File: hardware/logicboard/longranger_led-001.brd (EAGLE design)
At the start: 12.7 x 25.4 mm, 4 parts, among them J1 LED

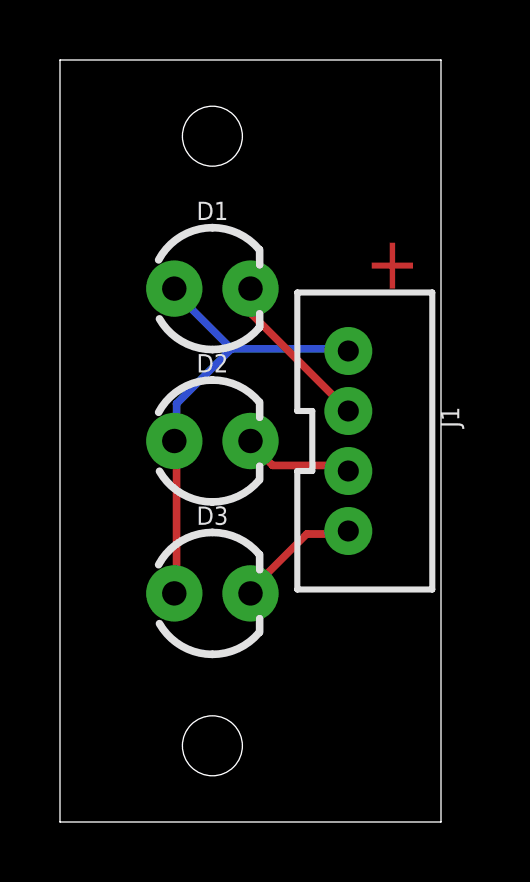
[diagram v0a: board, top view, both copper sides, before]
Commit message: Changed layout.
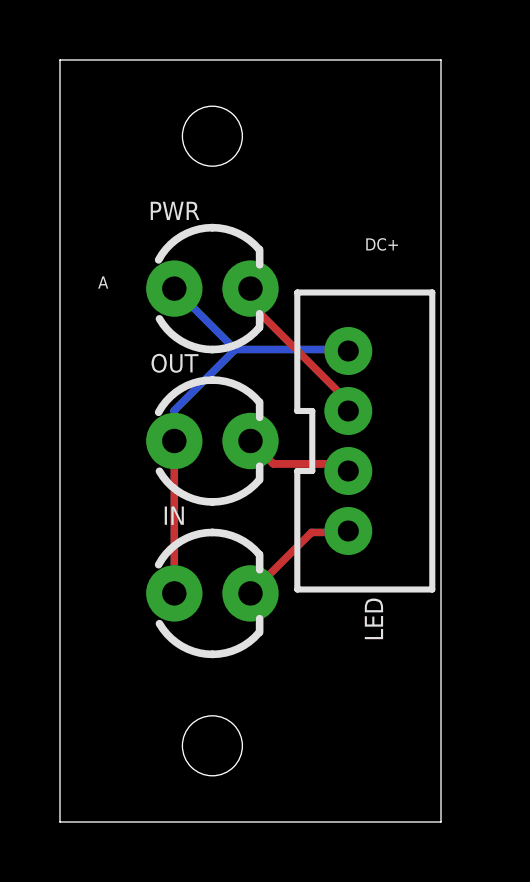
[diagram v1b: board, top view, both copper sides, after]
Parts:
- IN: value IN -> (none)
- LED: value LED -> (none)
- OUT: value OUT -> (none)
- PWR: value PWR -> (none)
- renumbered D1 to PWR, D2 to OUT, D3 to IN, J1 to LED
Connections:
- net N$4 renamed PWR
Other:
- board text added: "A"
- board text added: "DC+"
- board text removed: "+"
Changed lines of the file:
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@@
 <setting verticaltext="up"/>
 </settings>
-<grid distance="0.1" unitdist="inch" unit="inch" style="dots" multiple="1" display="yes" altdistance="0.025" altunitdist="inch" altunit="inch"/>
+<grid distance="50" unitdist="mil" unit="mil" style="lines" multiple="2" display="yes" altdistance="0.025" altunitdist="inch" altunit="inch"/>
 <layers>
 <layer number="1" name="Top" color="4" fill="1" visible="yes" active="yes"/>
@@
 <layer number="25" name="tNames" color="7" fill="1" visible="yes" active="yes"/>
 <layer number="26" name="bNames" color="7" fill="1" visible="yes" active="yes"/>
-<layer number="27" name="tValues" color="7" fill="1" visible="yes" active="yes"/>
-<layer number="28" name="bValues" color="7" fill="1" visible="yes" active="yes"/>
+<layer number="27" name="tValues" color="7" fill="1" visible="no" active="yes"/>
+<layer number="28" name="bValues" color="7" fill="1" visible="no" active="yes"/>
 <layer number="29" name="tStop" color="7" fill="3" visible="yes" active="yes"/>
 <layer number="30" name="bStop" color="7" fill="6" visible="yes" active="yes"/>
@@
 <hole x="5.08" y="2.54" drill="1.99898125"/>
 <hole x="5.08" y="22.86" drill="1.99898125"/>
-<text x="10.16" y="17.78" size="1.778" layer="1">+</text>
+<text x="10.16" y="19.05" size="0.4064" layer="25">DC+</text>
+<text x="1.27" y="17.78" size="0.4064" layer="25">A</text>
 </plain>
 <attributes>
@@
 </autorouter>
 <elements>
-<element name="J1" library="SparkFun-Connectors" package="JST-4-PTH-VERT" value="LED" x="10.16" y="12.7" rot="R270">
+<element name="LED" library="SparkFun-Connectors" package="JST-4-PTH-VERT" value="" x="10.16" y="12.7" smashed="yes" rot="R270">
+<attribute name="NAME" x="10.16" y="7.493" size="0.6096" layer="25" font="vector" ratio="20" rot="R270"/>
 <attribute name="PROD_ID" value="CONN-13251" x="10.16" y="12.7" size="1.778" layer="27" rot="R270" display="off"/>
+<attribute name="VALUE" x="6.858" y="14.351" size="0.6096" layer="27" font="vector" ratio="20" rot="R270"/>
 </element>
-<element name="D1" library="SparkFun-LED" package="LED_3MM" value="PWR" x="5.08" y="17.78">
+<element name="PWR" library="SparkFun-LED" package="LED_3MM" value="" x="5.08" y="17.78" smashed="yes">
+<attribute name="NAME" x="3.81" y="20.066" size="0.6096" layer="25" font="vector" ratio="20" align="bottom-center"/>
 <attribute name="PROD_ID" value="DIO-08794" x="5.08" y="17.78" size="1.778" layer="27" display="off"/>
+<attribute name="VALUE" x="5.08" y="15.494" size="0.6096" layer="27" font="vector" ratio="20" align="top-center"/>
 </element>
-<element name="D2" library="SparkFun-LED" package="LED_3MM" value="OUT" x="5.08" y="12.7">
+<element name="OUT" library="SparkFun-LED" package="LED_3MM" value="" x="5.08" y="12.7" smashed="yes">
+<attribute name="NAME" x="3.81" y="14.986" size="0.6096" layer="25" font="vector" ratio="20" align="bottom-center"/>
 <attribute name="PROD_ID" value="DIO-08794" x="5.08" y="12.7" size="1.778" layer="27" display="off"/>
+<attribute name="VALUE" x="5.08" y="10.414" size="0.6096" layer="27" font="vector" ratio="20" align="top-center"/>
 </element>
-<element name="D3" library="SparkFun-LED" package="LED_3MM" value="IN" x="5.08" y="7.62">
+<element name="IN" library="SparkFun-LED" package="LED_3MM" value="" x="5.08" y="7.62" smashed="yes">
+<attribute name="NAME" x="3.81" y="9.906" size="0.6096" layer="25" font="vector" ratio="20" align="bottom-center"/>
 <attribute name="PROD_ID" value="DIO-08794" x="5.08" y="7.62" size="1.778" layer="27" display="off"/>
+<attribute name="VALUE" x="5.08" y="5.334" size="0.6096" layer="27" font="vector" ratio="20" align="top-center"/>
 </element>
 </elements>
 <signals>
-<signal name="N$4">
-<contactref element="J1" pad="1"/>
-<contactref element="D3" pad="A"/>
-<contactref element="D2" pad="A"/>
-<contactref element="D1" pad="A"/>
-<wire x1="3.8862" y1="12.573" x2="3.8862" y2="7.7724" width="0.254" layer="1"/>
-<wire x1="3.8862" y1="7.7724" x2="3.81" y2="7.62" width="0.254" layer="1"/>
-<wire x1="3.8862" y1="12.573" x2="3.81" y2="12.7" width="0.254" layer="1"/>
-<wire x1="5.715" y1="15.7734" x2="9.6012" y2="15.7734" width="0.254" layer="16"/>
-<wire x1="3.8862" y1="17.6022" x2="5.715" y2="15.7734" width="0.254" layer="16"/>
-<wire x1="9.6012" y1="15.7734" x2="9.61" y2="15.7" width="0.254" layer="16"/>
-<wire x1="3.8862" y1="17.6022" x2="3.81" y2="17.78" width="0.254" layer="16"/>
-<wire x1="3.8862" y1="13.9446" x2="3.8862" y2="12.8016" width="0.254" layer="16"/>
-<wire x1="5.715" y1="15.7734" x2="3.8862" y2="13.9446" width="0.254" layer="16"/>
-<wire x1="3.8862" y1="12.8016" x2="3.81" y2="12.7" width="0.254" layer="16"/>
+<signal name="PWR">
+<contactref element="LED" pad="1"/>
+<contactref element="IN" pad="A"/>
+<contactref element="OUT" pad="A"/>
+<contactref element="PWR" pad="A"/>
+<wire x1="3.81" y1="12.7" x2="3.81" y2="7.62" width="0.254" layer="1"/>
+<wire x1="5.842" y1="15.748" x2="9.398" y2="15.748" width="0.254" layer="16"/>
+<wire x1="3.81" y1="17.78" x2="5.842" y2="15.748" width="0.254" layer="16"/>
+<wire x1="9.398" y1="15.748" x2="9.61" y2="15.7" width="0.254" layer="16"/>
+<wire x1="3.81" y1="13.716" x2="3.81" y2="12.7" width="0.254" layer="16"/>
+<wire x1="5.842" y1="15.748" x2="3.81" y2="13.716" width="0.254" layer="16"/>
 </signal>
 <signal name="N$5">
-<contactref element="J1" pad="2"/>
-<contactref element="D1" pad="K"/>
-<wire x1="6.4008" y1="16.9164" x2="9.6012" y2="13.716" width="0.254" layer="1"/>
-<wire x1="6.4008" y1="17.6022" x2="6.4008" y2="16.9164" width="0.254" layer="1"/>
-<wire x1="9.6012" y1="13.716" x2="9.61" y2="13.7" width="0.254" layer="1"/>
-<wire x1="6.4008" y1="17.6022" x2="6.35" y2="17.78" width="0.254" layer="1"/>
+<contactref element="LED" pad="2"/>
+<contactref element="PWR" pad="K"/>
+<wire x1="9.398" y1="14.224" x2="9.398" y2="13.716" width="0.254" layer="1"/>
+<wire x1="6.35" y1="17.272" x2="9.398" y2="14.224" width="0.254" layer="1"/>
+<wire x1="6.35" y1="17.78" x2="6.35" y2="17.272" width="0.254" layer="1"/>
+<wire x1="9.398" y1="13.716" x2="9.61" y2="13.7" width="0.254" layer="1"/>
 </signal>
 <signal name="N$11">
-<contactref element="J1" pad="3"/>
-<contactref element="D2" pad="K"/>
-<wire x1="7.0866" y1="11.8872" x2="9.6012" y2="11.8872" width="0.254" layer="1"/>
-<wire x1="6.4008" y1="12.573" x2="7.0866" y2="11.8872" width="0.254" layer="1"/>
-<wire x1="9.6012" y1="11.8872" x2="9.61" y2="11.7" width="0.254" layer="1"/>
-<wire x1="6.4008" y1="12.573" x2="6.35" y2="12.7" width="0.254" layer="1"/>
+<contactref element="LED" pad="3"/>
+<contactref element="OUT" pad="K"/>
+<wire x1="7.112" y1="11.938" x2="9.398" y2="11.938" width="0.254" layer="1"/>
+<wire x1="6.35" y1="12.7" x2="7.112" y2="11.938" width="0.254" layer="1"/>
+<wire x1="9.398" y1="11.938" x2="9.61" y2="11.7" width="0.254" layer="1"/>
 </signal>
 <signal name="N$12">
-<contactref element="J1" pad="4"/>
-<contactref element="D3" pad="K"/>
-<wire x1="8.2296" y1="9.6012" x2="9.6012" y2="9.6012" width="0.254" layer="1"/>
-<wire x1="6.4008" y1="7.7724" x2="8.2296" y2="9.6012" width="0.254" layer="1"/>
-<wire x1="9.6012" y1="9.6012" x2="9.61" y2="9.7" width="0.254" layer="1"/>
-<wire x1="6.4008" y1="7.7724" x2="6.35" y2="7.62" width="0.254" layer="1"/>
+<contactref element="LED" pad="4"/>
+<contactref element="IN" pad="K"/>
+<wire x1="8.382" y1="9.652" x2="9.398" y2="9.652" width="0.254" layer="1"/>
+<wire x1="6.35" y1="7.62" x2="8.382" y2="9.652" width="0.254" layer="1"/>
+<wire x1="9.398" y1="9.652" x2="9.61" y2="9.7" width="0.254" layer="1"/>
 </signal>
 </signals>

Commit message: Changed LED pitch.
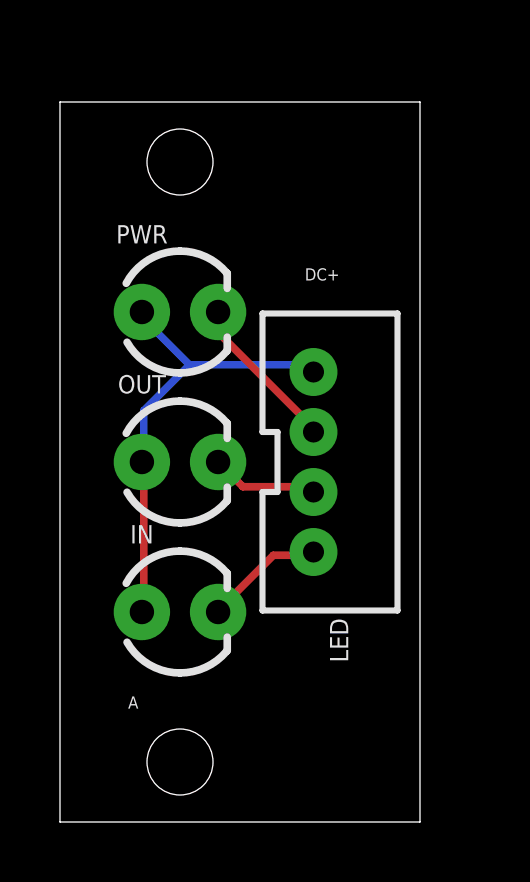
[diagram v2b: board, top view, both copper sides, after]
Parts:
- moved LED 1.35 mm to (9.00, 12.0)
- moved PWR 1.33 mm to (4.00, 17.0)
- moved OUT 1.29 mm to (4.00, 12.0)
- moved IN 1.25 mm to (4.00, 7.00)
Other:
- board size 12.7 x 25.4 mm -> 12 x 24 mm
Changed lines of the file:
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@@
 <setting verticaltext="up"/>
 </settings>
-<grid distance="50" unitdist="mil" unit="mil" style="lines" multiple="2" display="yes" altdistance="0.025" altunitdist="inch" altunit="inch"/>
+<grid distance="1" unitdist="mm" unit="mm" style="lines" multiple="2" display="yes" altdistance="0.025" altunitdist="inch" altunit="inch"/>
 <layers>
 <layer number="1" name="Top" color="4" fill="1" visible="yes" active="yes"/>
@@
 <board>
 <plain>
-<wire x1="0" y1="0" x2="12.7" y2="0" width="0" layer="20"/>
-<wire x1="12.7" y1="0" x2="12.7" y2="25.4" width="0" layer="20"/>
-<wire x1="12.7" y1="25.4" x2="0" y2="25.4" width="0" layer="20"/>
-<wire x1="0" y1="25.4" x2="0" y2="0" width="0" layer="20"/>
-<hole x="5.08" y="2.54" drill="1.99898125"/>
-<hole x="5.08" y="22.86" drill="1.99898125"/>
-<text x="10.16" y="19.05" size="0.4064" layer="25">DC+</text>
-<text x="1.27" y="17.78" size="0.4064" layer="25">A</text>
+<wire x1="0" y1="0" x2="12" y2="0" width="0" layer="20"/>
+<wire x1="12" y1="0" x2="12" y2="24" width="0" layer="20"/>
+<wire x1="12" y1="24" x2="0" y2="24" width="0" layer="20"/>
+<wire x1="0" y1="24" x2="0" y2="0" width="0" layer="20"/>
+<hole x="4" y="2" drill="2.2"/>
+<hole x="4" y="22" drill="2.2"/>
+<text x="8.16" y="18.05" size="0.4064" layer="25">DC+</text>
+<text x="2.27" y="3.78" size="0.4064" layer="25">A</text>
 </plain>
 <attributes>
@@
 </variantdefs>
 <classes>
-<class number="0" name="default" width="0" drill="0">
+<class number="0" name="default" width="0.127" drill="0.127">
+<clearance class="0" value="0.127"/>
 </class>
 </classes>
-<designrules name="default">
+<designrules name="default *">
 <description language="de">&lt;b&gt;EAGLE Design Rules&lt;/b&gt;
 &lt;p&gt;
@@
 <param name="mtCopper" value="0.035mm 0.035mm 0.035mm 0.035mm 0.035mm 0.035mm 0.035mm 0.035mm 0.035mm 0.035mm 0.035mm 0.035mm 0.035mm 0.035mm 0.035mm 0.035mm"/>
 <param name="mtIsolate" value="1.5mm 0.15mm 0.2mm 0.15mm 0.2mm 0.15mm 0.2mm 0.15mm 0.2mm 0.15mm 0.2mm 0.15mm 0.2mm 0.15mm 0.2mm"/>
-<param name="mdWireWire" value="8mil"/>
-<param name="mdWirePad" value="8mil"/>
-<param name="mdWireVia" value="8mil"/>
-<param name="mdPadPad" value="8mil"/>
-<param name="mdPadVia" value="8mil"/>
-<param name="mdViaVia" value="8mil"/>
+<param name="mdWireWire" value="10mil"/>
+<param name="mdWirePad" value="10mil"/>
+<param name="mdWireVia" value="10mil"/>
+<param name="mdPadPad" value="10mil"/>
+<param name="mdPadVia" value="10mil"/>
+<param name="mdViaVia" value="10mil"/>
 <param name="mdSmdPad" value="8mil"/>
 <param name="mdSmdVia" value="8mil"/>
@@
 </autorouter>
 <elements>
-<element name="LED" library="SparkFun-Connectors" package="JST-4-PTH-VERT" value="" x="10.16" y="12.7" smashed="yes" rot="R270">
-<attribute name="NAME" x="10.16" y="7.493" size="0.6096" layer="25" font="vector" ratio="20" rot="R270"/>
-<attribute name="PROD_ID" value="CONN-13251" x="10.16" y="12.7" size="1.778" layer="27" rot="R270" display="off"/>
-<attribute name="VALUE" x="6.858" y="14.351" size="0.6096" layer="27" font="vector" ratio="20" rot="R270"/>
+<element name="LED" library="SparkFun-Connectors" package="JST-4-PTH-VERT" value="" x="9" y="12" smashed="yes" rot="R270">
+<attribute name="NAME" x="9" y="6.793" size="0.6096" layer="25" font="vector" ratio="20" rot="R270"/>
+<attribute name="PROD_ID" value="CONN-13251" x="9" y="12" size="1.778" layer="27" rot="R270" display="off"/>
+<attribute name="VALUE" x="5.698" y="13.651" size="0.6096" layer="27" font="vector" ratio="20" rot="R270"/>
 </element>
-<element name="PWR" library="SparkFun-LED" package="LED_3MM" value="" x="5.08" y="17.78" smashed="yes">
-<attribute name="NAME" x="3.81" y="20.066" size="0.6096" layer="25" font="vector" ratio="20" align="bottom-center"/>
-<attribute name="PROD_ID" value="DIO-08794" x="5.08" y="17.78" size="1.778" layer="27" display="off"/>
-<attribute name="VALUE" x="5.08" y="15.494" size="0.6096" layer="27" font="vector" ratio="20" align="top-center"/>
+<element name="PWR" library="SparkFun-LED" package="LED_3MM" value="" x="4" y="17" smashed="yes">
+<attribute name="NAME" x="2.73" y="19.286" size="0.6096" layer="25" font="vector" ratio="20" align="bottom-center"/>
+<attribute name="PROD_ID" value="DIO-08794" x="4" y="17" size="1.778" layer="27" display="off"/>
+<attribute name="VALUE" x="4" y="14.714" size="0.6096" layer="27" font="vector" ratio="20" align="top-center"/>
 </element>
-<element name="OUT" library="SparkFun-LED" package="LED_3MM" value="" x="5.08" y="12.7" smashed="yes">
-<attribute name="NAME" x="3.81" y="14.986" size="0.6096" layer="25" font="vector" ratio="20" align="bottom-center"/>
-<attribute name="PROD_ID" value="DIO-08794" x="5.08" y="12.7" size="1.778" layer="27" display="off"/>
-<attribute name="VALUE" x="5.08" y="10.414" size="0.6096" layer="27" font="vector" ratio="20" align="top-center"/>
+<element name="OUT" library="SparkFun-LED" package="LED_3MM" value="" x="4" y="12" smashed="yes">
+<attribute name="NAME" x="2.73" y="14.286" size="0.6096" layer="25" font="vector" ratio="20" align="bottom-center"/>
+<attribute name="PROD_ID" value="DIO-08794" x="4" y="12" size="1.778" layer="27" display="off"/>
+<attribute name="VALUE" x="4" y="9.714" size="0.6096" layer="27" font="vector" ratio="20" align="top-center"/>
 </element>
-<element name="IN" library="SparkFun-LED" package="LED_3MM" value="" x="5.08" y="7.62" smashed="yes">
-<attribute name="NAME" x="3.81" y="9.906" size="0.6096" layer="25" font="vector" ratio="20" align="bottom-center"/>
-<attribute name="PROD_ID" value="DIO-08794" x="5.08" y="7.62" size="1.778" layer="27" display="off"/>
-<attribute name="VALUE" x="5.08" y="5.334" size="0.6096" layer="27" font="vector" ratio="20" align="top-center"/>
+<element name="IN" library="SparkFun-LED" package="LED_3MM" value="" x="4" y="7" smashed="yes">
+<attribute name="NAME" x="2.73" y="9.286" size="0.6096" layer="25" font="vector" ratio="20" align="bottom-center"/>
+<attribute name="PROD_ID" value="DIO-08794" x="4" y="7" size="1.778" layer="27" display="off"/>
+<attribute name="VALUE" x="4" y="4.714" size="0.6096" layer="27" font="vector" ratio="20" align="top-center"/>
 </element>
 </elements>
@@
 <contactref element="OUT" pad="A"/>
 <contactref element="PWR" pad="A"/>
-<wire x1="3.81" y1="12.7" x2="3.81" y2="7.62" width="0.254" layer="1"/>
-<wire x1="5.842" y1="15.748" x2="9.398" y2="15.748" width="0.254" layer="16"/>
-<wire x1="3.81" y1="17.78" x2="5.842" y2="15.748" width="0.254" layer="16"/>
-<wire x1="9.398" y1="15.748" x2="9.61" y2="15.7" width="0.254" layer="16"/>
-<wire x1="3.81" y1="13.716" x2="3.81" y2="12.7" width="0.254" layer="16"/>
-<wire x1="5.842" y1="15.748" x2="3.81" y2="13.716" width="0.254" layer="16"/>
+<wire x1="2.794" y1="11.938" x2="2.794" y2="7.112" width="0.254" layer="1"/>
+<wire x1="2.794" y1="7.112" x2="2.73" y2="7" width="0.254" layer="1"/>
+<wire x1="2.794" y1="11.938" x2="2.73" y2="12" width="0.254" layer="1"/>
+<wire x1="4.318" y1="15.24" x2="8.382" y2="15.24" width="0.254" layer="16"/>
+<wire x1="2.794" y1="16.764" x2="4.318" y2="15.24" width="0.254" layer="16"/>
+<wire x1="8.382" y1="15.24" x2="8.45" y2="15" width="0.254" layer="16"/>
+<wire x1="2.794" y1="16.764" x2="2.73" y2="17" width="0.254" layer="16"/>
+<wire x1="2.794" y1="13.716" x2="2.794" y2="12.192" width="0.254" layer="16"/>
+<wire x1="4.318" y1="15.24" x2="2.794" y2="13.716" width="0.254" layer="16"/>
+<wire x1="2.794" y1="12.192" x2="2.73" y2="12" width="0.254" layer="16"/>
 </signal>
 <signal name="N$5">
 <contactref element="LED" pad="2"/>
 <contactref element="PWR" pad="K"/>
-<wire x1="9.398" y1="14.224" x2="9.398" y2="13.716" width="0.254" layer="1"/>
-<wire x1="6.35" y1="17.272" x2="9.398" y2="14.224" width="0.254" layer="1"/>
-<wire x1="6.35" y1="17.78" x2="6.35" y2="17.272" width="0.254" layer="1"/>
-<wire x1="9.398" y1="13.716" x2="9.61" y2="13.7" width="0.254" layer="1"/>
+<wire x1="5.334" y1="16.256" x2="8.382" y2="13.208" width="0.254" layer="1"/>
+<wire x1="5.334" y1="16.764" x2="5.334" y2="16.256" width="0.254" layer="1"/>
+<wire x1="8.382" y1="13.208" x2="8.45" y2="13" width="0.254" layer="1"/>
+<wire x1="5.334" y1="16.764" x2="5.27" y2="17" width="0.254" layer="1"/>
 </signal>
 <signal name="N$11">
 <contactref element="LED" pad="3"/>
 <contactref element="OUT" pad="K"/>
-<wire x1="7.112" y1="11.938" x2="9.398" y2="11.938" width="0.254" layer="1"/>
-<wire x1="6.35" y1="12.7" x2="7.112" y2="11.938" width="0.254" layer="1"/>
-<wire x1="9.398" y1="11.938" x2="9.61" y2="11.7" width="0.254" layer="1"/>
+<wire x1="6.096" y1="11.176" x2="8.382" y2="11.176" width="0.254" layer="1"/>
+<wire x1="5.334" y1="11.938" x2="6.096" y2="11.176" width="0.254" layer="1"/>
+<wire x1="8.382" y1="11.176" x2="8.45" y2="11" width="0.254" layer="1"/>
+<wire x1="5.334" y1="11.938" x2="5.27" y2="12" width="0.254" layer="1"/>
 </signal>
 <signal name="N$12">
 <contactref element="LED" pad="4"/>
 <contactref element="IN" pad="K"/>
-<wire x1="8.382" y1="9.652" x2="9.398" y2="9.652" width="0.254" layer="1"/>
-<wire x1="6.35" y1="7.62" x2="8.382" y2="9.652" width="0.254" layer="1"/>
-<wire x1="9.398" y1="9.652" x2="9.61" y2="9.7" width="0.254" layer="1"/>
+<wire x1="7.112" y1="8.89" x2="8.382" y2="8.89" width="0.254" layer="1"/>
+<wire x1="5.334" y1="7.112" x2="7.112" y2="8.89" width="0.254" layer="1"/>
+<wire x1="8.382" y1="8.89" x2="8.45" y2="9" width="0.254" layer="1"/>
+<wire x1="5.334" y1="7.112" x2="5.27" y2="7" width="0.254" layer="1"/>
 </signal>
 </signals>
